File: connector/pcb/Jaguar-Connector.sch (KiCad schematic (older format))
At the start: 39 parts, among them J1 TE-776163, P1 FUEL-12v, P10 O2-GND, P11 TPS-GND, P12 INJ-7, P13 INJ-8, P14 INJ-GND, P15 BRV-12v, P16 CRANK+, P17 CAM+, P18 TPS-5v, P19 TPS, P2 FAN-12v, P20 O2, P21 IAT, P22 MAT, P23 COOLANT, P24 MAF-Signal, P25 INJ-1, P26 INJ-2, P27 INJ-3, P28 CRANK-, P29 CAM-, P3 ACC-12v, P30 OUT-GND, P31 ACC-, P32 FAN-, P33 FUEL-, P34 IGN-ADVANCE, P35 DIS-BYPASS, P36 INJ-4, P37 INJ-5, P38 INJ-6, P4 12vdc, P5 12vdc, P6 12v-SW, P7 12v-SW2, P8 GND, P9 GND2

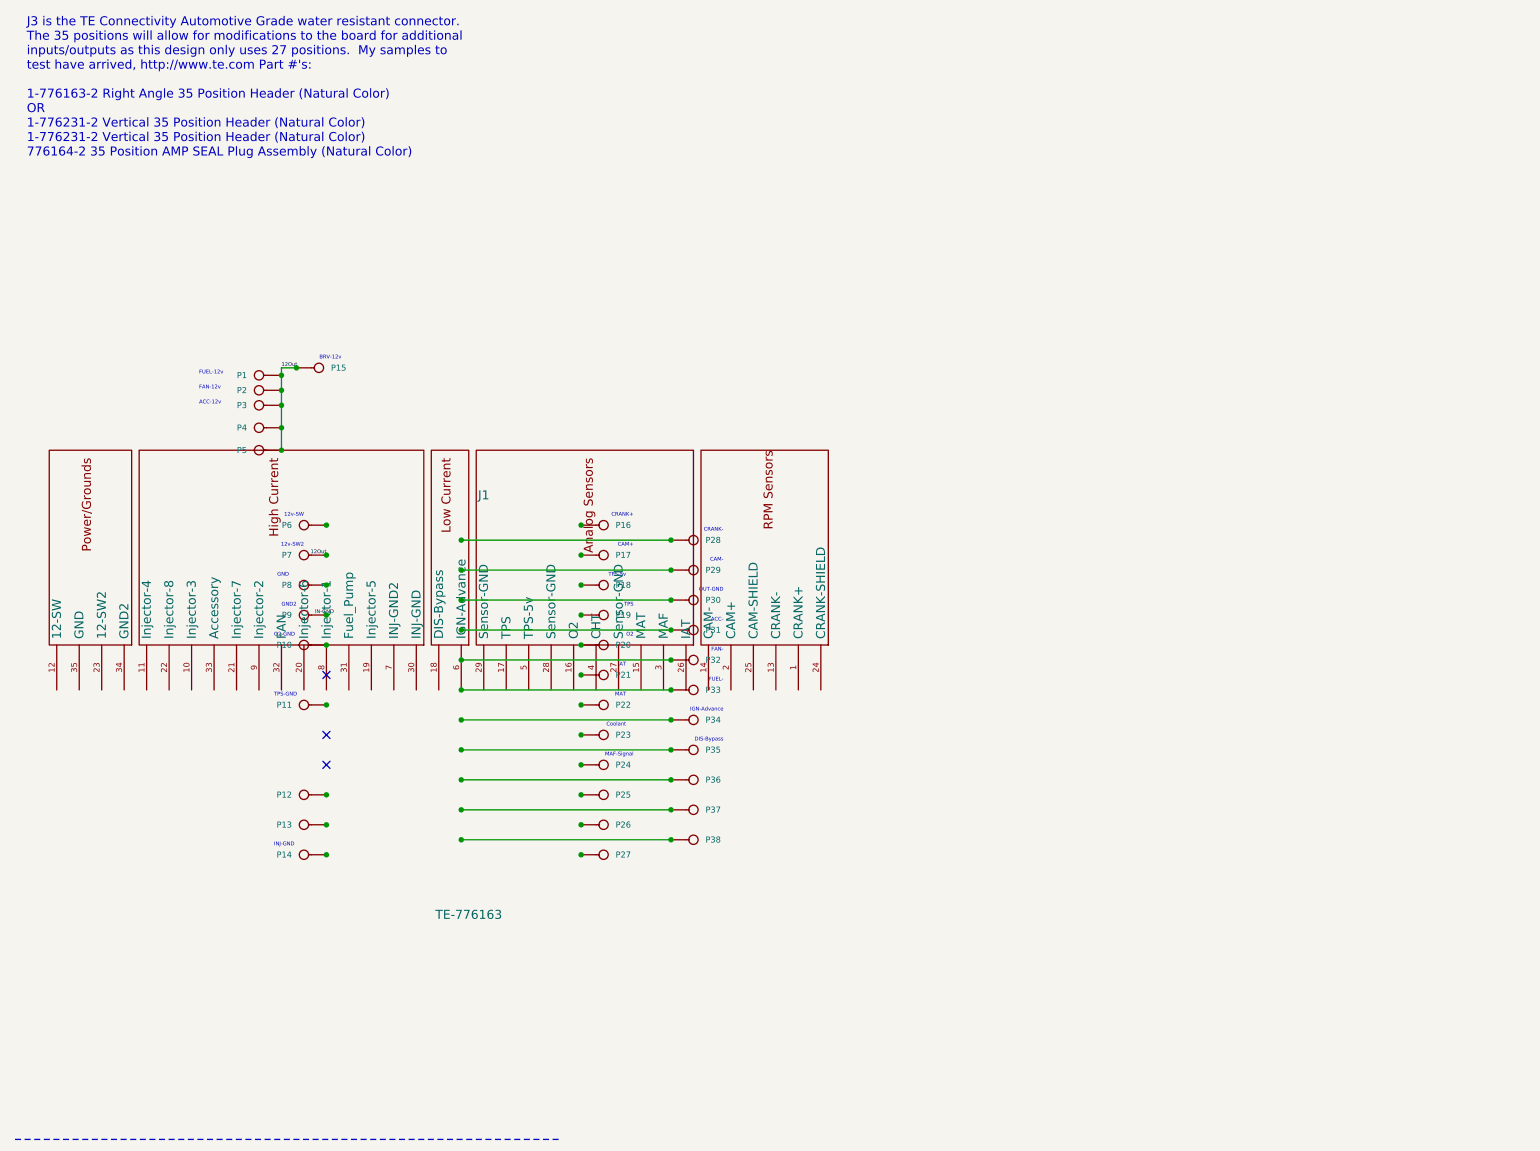
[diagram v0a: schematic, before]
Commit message: Edited Connector, created all new PDFs
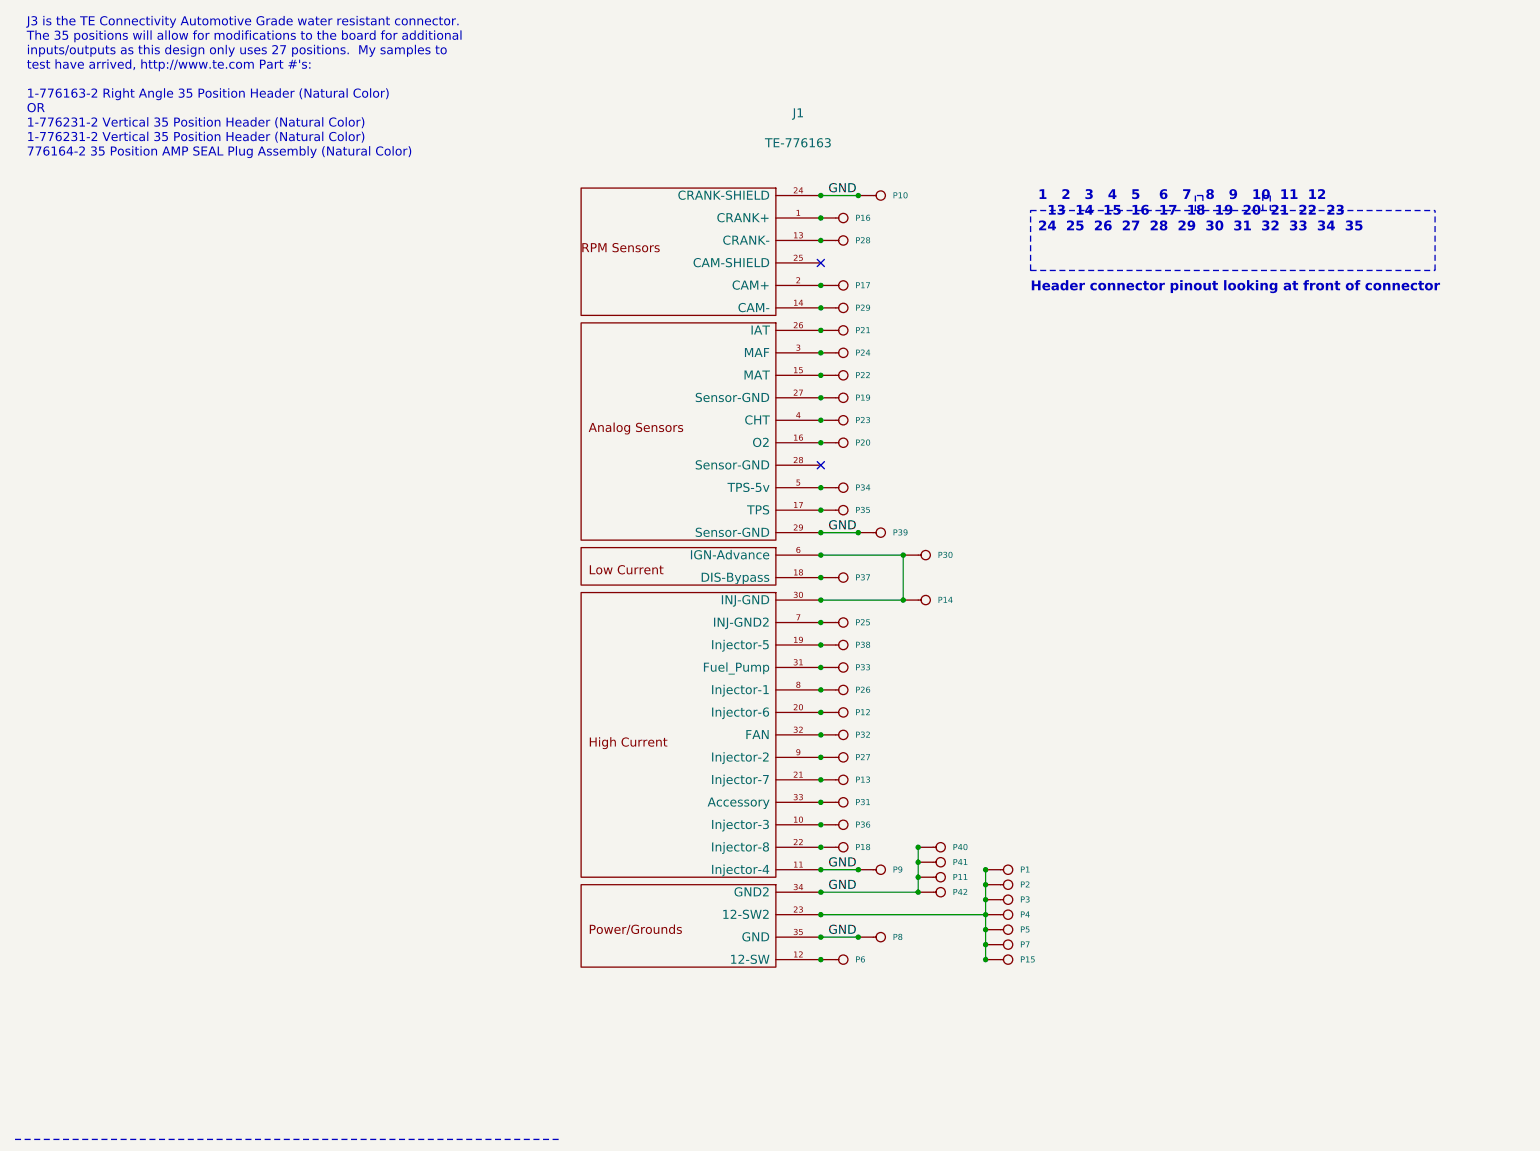
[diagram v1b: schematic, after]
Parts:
- added P39: IGN-GND, symbol CONN_1
- added P40, P41, P42: Sensor-GND, symbol CONN_1
- P10: value O2-GND -> VR-SHIELD
- P11: value TPS-GND -> Sensor-GND
- P23: value COOLANT -> CHT
- P30: value OUT-GND -> INJ-GND2
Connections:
- net 12Out is gone; now on an unnamed net: P1.1, P15.1, P2.1, P3.1, P4.1, P5.1, P7.1
- net at P6.1: now also J1.12 (12-SW)
- net at P35.1: now also J1.17 (TPS)
- net at P34.1: now also J1.5 (TPS-5v)
- net at P21.1: now also J1.26 (IAT)
- net at P22.1: now also J1.15 (MAT)
- net at P23.1: now also J1.4 (CHT)
- net at P19.1: now also J1.27 (Sensor-GND)
- net GND: now reaches P11.1
- net GND: now also J1.11 (Injector-4), J1.24 (CRANK-SHIELD), J1.29 (Sensor-GND), J1.34 (GND2), J1.35 (GND), P10.1, P8.1, P9.1, P39.1, P40.1, P41.1, P42.1
- net at P20.1: now also J1.16 (O2)
- net at P16.1: now also J1.1 (CRANK+)
- net at P33.1: now also J1.31 (Fuel_Pump); no longer J1.6 (IGN-Advance)
- net at P17.1: now also J1.2 (CAM+)
- net at P29.1: now also J1.14 (CAM-)
- net at P14.1: now also J1.30 (INJ-GND), J1.6 (IGN-Advance), P30.1
- net at P28.1: now also J1.13 (CRANK-)
- net at P18.1: now also J1.22 (Injector-8)
- net at P32.1: now also J1.32 (FAN)
- net at P31.1: now also J1.33 (Accessory)
- net at P24.1: now also J1.3 (MAF)
- net at J1.10 (Injector-3): now also P36.1
- net at J1.18 (DIS-Bypass): now also P37.1
- net at J1.19 (Injector-5): now also P38.1
- net at J1.20 (Injector-6): now also P12.1
- net at J1.21 (Injector-7): now also P13.1
- net at J1.7 (INJ-GND2): now also P25.1
- net at J1.8 (Injector-1): now also P26.1
- net at J1.9 (Injector-2): now also P27.1
- no-connect marks 3 -> 2
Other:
- note added: "1 2 3 4 5 6 7 8 9 10 11 12\n 13 14 15 16 17 18 19 20 21 22 23\n24 25 26 27 28 29 30 31 32 33 34 35"
- note added: "Header connector pinout looking at front of connector"
- note removed: "12v-SW"
- note removed: "12v-SW2"
- note removed: "ACC-"
- note removed: "ACC-12v"
- note removed: "BRV-12v"
- note removed: "CAM+"
- note removed: "CAM-"
- note removed: "CRANK+"
- note removed: "CRANK-"
- note removed: "Coolant"
- note removed: "DIS-Bypass"
- note removed: "FAN-"
- note removed: "FAN-12v"
- note removed: "FUEL-"
- note removed: "FUEL-12v"
- note removed: "GND"
- note removed: "GND2"
- note removed: "IAT"
- note removed: "IGN-Advance"
- note removed: "INJ-GND"
- note removed: "MAF-Signal"
- note removed: "MAT"
- note removed: "O2"
- note removed: "O2-GND"
- note removed: "OUT-GND"
- note removed: "TPS"
- note removed: "TPS-5v"
- note removed: "TPS-GND"
- moved on the sheet: P1, P10, P11, P12, P13, P14, P15, P16, P17, P18, P19, P2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

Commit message: Revised /docs/Connector-Schematic.pdf
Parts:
- added P43: CAM-SHIELD, symbol CONN_1
- P10: value VR-SHIELD -> CRANK-SHIELD
- P39: value IGN-GND -> Sensor/EST-GND
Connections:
- net GND: now also J1.25 (CAM-SHIELD), J1.27 (Sensor-GND), J1.28 (Sensor-GND), P43.1; no longer J1.11 (Injector-4)
- net at P35.1: now also J1.18 (DIS-Bypass); no longer J1.17 (TPS)
- net at P34.1: now also J1.6 (IGN-Advance); no longer J1.5 (TPS-5v)
- net at P19.1: now also J1.17 (TPS); no longer J1.27 (Sensor-GND)
- net INJ-GND: now reaches J1.30 (INJ-GND), P14.1, P30.1
- net INJ-GND: now also J1.7 (INJ-GND2); no longer J1.6 (IGN-Advance)
- net at P18.1: now also J1.5 (TPS-5v); no longer J1.22 (Injector-8)
- net at P27.1: now also J1.10 (Injector-3); no longer J1.9 (Injector-2)
- net at P38.1: now also J1.20 (Injector-6); no longer J1.19 (Injector-5)
- net at P37.1: now also J1.19 (Injector-5); no longer J1.18 (DIS-Bypass)
- net at P26.1: now also J1.9 (Injector-2); no longer J1.8 (Injector-1)
- net at P36.1: now also J1.11 (Injector-4); no longer J1.10 (Injector-3)
- net at P12.1: now also J1.21 (Injector-7); no longer J1.20 (Injector-6)
- net at P13.1: now also J1.22 (Injector-8); no longer J1.21 (Injector-7)
- net at P25.1: now also J1.8 (Injector-1); no longer J1.7 (INJ-GND2)
- no-connect marks 2 -> 0
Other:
- moved on the sheet: P1, P11, P12, P13, P14, P15, P18, P19, P2, P25, P26, P27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

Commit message: Updated Connector to remove EST-GND from Sensor-GND
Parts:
- P39: value Sensor/EST-GND -> Sensor-GND
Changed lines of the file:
@@
-EESchema Schematic File Version 2  date Wed 01 Feb 2012 11:24:33 AM EST
+EESchema Schematic File Version 2  date Wed 01 Feb 2012 01:47:51 PM EST
 LIBS:power
 LIBS:device
@@
 P 6350 3700
 F 0 "P39" H 6430 3700 40  0000 L CNN
-F 1 "Sensor/EST-GND" H 6350 3755 30  0001 C CNN
+F 1 "Sensor-GND" H 6350 3755 30  0001 C CNN
 	1    6350 3700
 	1    0    0    -1
